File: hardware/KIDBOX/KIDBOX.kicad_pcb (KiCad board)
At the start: 2 copper layers, 150 x 65 mm, 0 parts

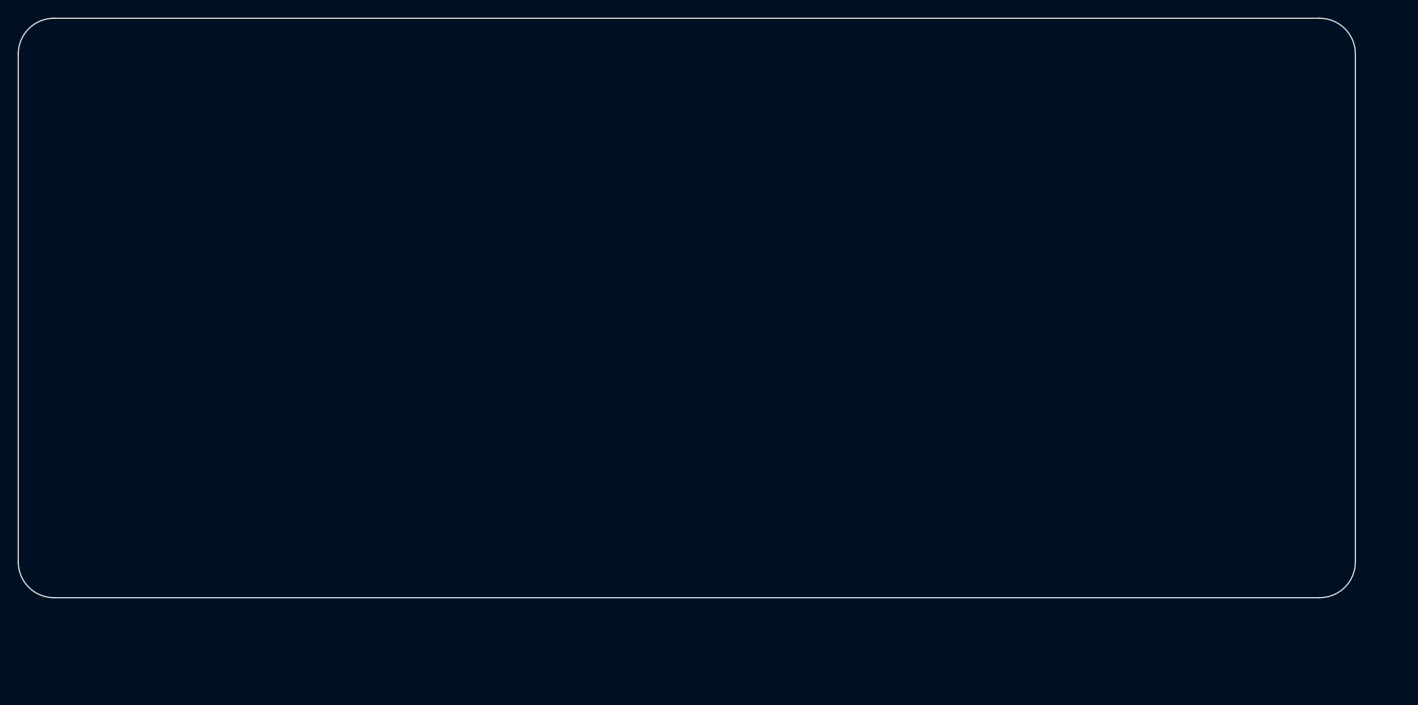
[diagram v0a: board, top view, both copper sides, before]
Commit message: Fase 2 PCB KIDBOX + correcciones de revision (sin H5/H6, SELECT/START a 66.5/83.5)
- scripts/gen_pcb.py: PCB completo generado con pcbnew (contorno 150x65 r4,
  H1-H4, huellas oficiales en las posiciones de la seccion 6, 0 vias, pistas
  en F.Cu, plano GND continuo en B.Cu con alivios termicos, serigrafia).
- J5 con VIN a la derecha visto de frente (I2S sin cruces ni vias); 3V3 a
  VIN por un puente pad a pad en B.Cu; PWR_EN por el borde superior.
- Revision del alumno: se eliminan H5/H6 y la regla de KIDBOX.kicad_dru;
  SW5/SW6 a x = 66.5 / 83.5 para sacar el cobre de START de la zona de bateria.
- verificar.py: ERC 0, DRC 0 errores / 0 avisos, 0 sin conectar, paridad 0.

Co-Authored-By: Claude Opus 5.5 <noreply@anthropic.com>
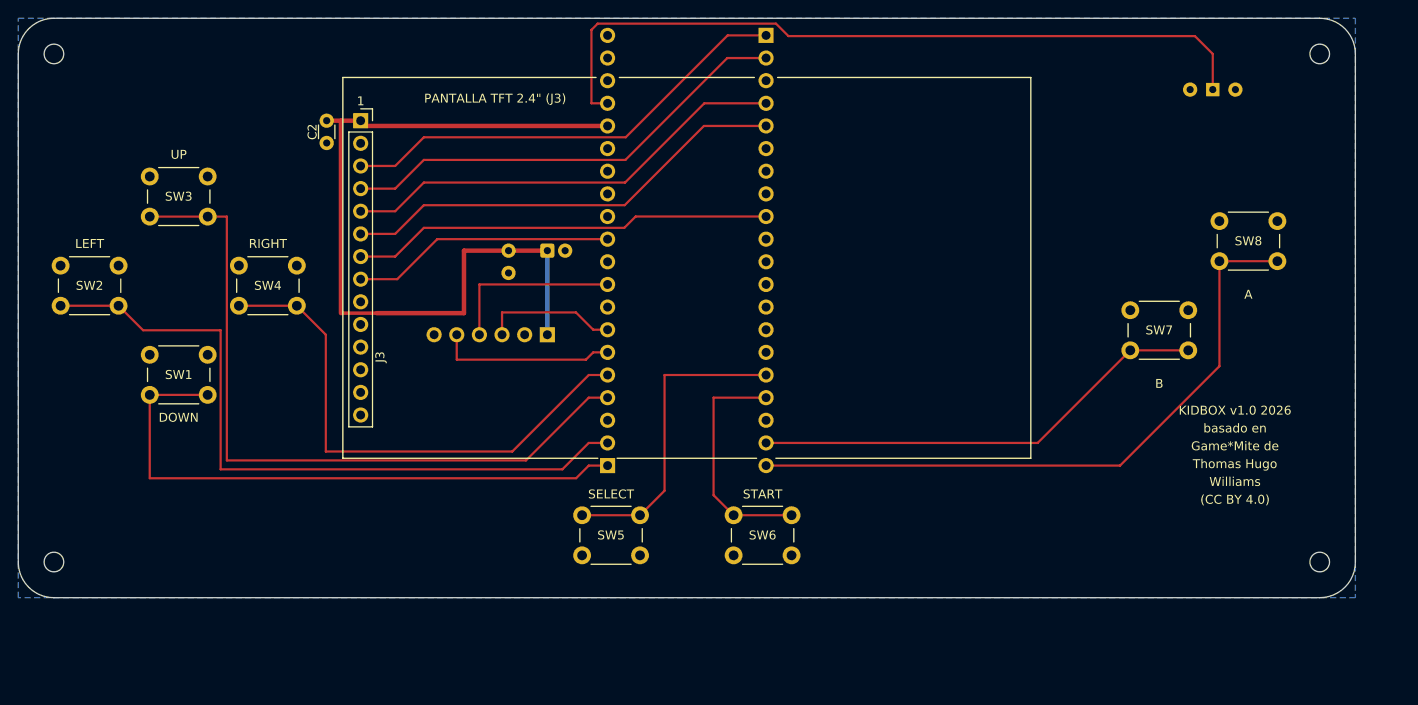
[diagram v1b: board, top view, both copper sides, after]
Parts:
- added C2: 100n, Capacitor_THT:C_Disc_D3.0mm_W1.6mm_P2.50mm, F.Cu at (34.6, 11.5)
- added C3: 100n, Capacitor_THT:C_Disc_D3.0mm_W1.6mm_P2.50mm, B.Cu at (55.0, 26.1)
- added C4: 10u 16V, Capacitor_THT:CP_Radial_D5.0mm_P2.00mm, B.Cu at (59.4, 26.1)
- added H1: M2, MountingHole:MountingHole_2.2mm_M2, F.Cu at (4.00, 4.00)
- added H2: M2, MountingHole:MountingHole_2.2mm_M2, F.Cu at (146.0, 4.00)
- added H3: M2, MountingHole:MountingHole_2.2mm_M2, F.Cu at (4.00, 61.0)
- added H4: M2, MountingHole:MountingHole_2.2mm_M2, F.Cu at (146.0, 61.0)
- added J1: RP2350-Plus 1-20, Connector_PinSocket_2.54mm:PinSocket_1x20_P2.54mm_Vertical, B.Cu at (83.9, 1.92)
- added J2: RP2350-Plus 21-40, Connector_PinSocket_2.54mm:PinSocket_1x20_P2.54mm_Vertical, B.Cu at (66.1, 50.2)
- added J3: TFT ILI9341 2.4in, Connector_PinSocket_2.54mm:PinSocket_1x14_P2.54mm_Vertical, F.Cu at (38.4, 11.5)
- added J5: DAC GY-PCM5102, Connector_PinSocket_2.54mm:PinSocket_1x06_P2.54mm_Vertical, B.Cu at (59.4, 35.5)
- added SW1: DOWN, Button_Switch_THT:SW_PUSH_6mm, F.Cu at (21.2, 42.2)
- added SW10: ON/OFF, Button_Switch_THT:SW_Slide-03_Wuerth-WS-SLTV_10x2.5x6.4_P2.54mm, B.Cu at (134.0, 8.00)
- added SW2: LEFT, Button_Switch_THT:SW_PUSH_6mm, F.Cu at (11.2, 32.2)
- added SW3: UP, Button_Switch_THT:SW_PUSH_6mm, F.Cu at (21.2, 22.2)
- added SW4: RIGHT, Button_Switch_THT:SW_PUSH_6mm, F.Cu at (31.2, 32.2)
- added SW5: SELECT, Button_Switch_THT:SW_PUSH_6mm, F.Cu at (63.2, 55.8)
- added SW6: START, Button_Switch_THT:SW_PUSH_6mm, F.Cu at (80.2, 55.8)
- added SW7: B, Button_Switch_THT:SW_PUSH_6mm, F.Cu at (131.2, 37.2)
- added SW8: A, Button_Switch_THT:SW_PUSH_6mm, F.Cu at (141.2, 27.2)
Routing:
- net +3V3: track 0.00 -> 92.9 mm
- net /PWR_EN: track 0.00 -> 85.4 mm
- net /BTN_UP: track 0.00 -> 81.6 mm
- net /BTN_LEFT: track 0.00 -> 79.3 mm
- net /BTN_A: track 0.00 -> 73.8 mm
- net /BTN_DOWN: track 0.00 -> 67.8 mm
- net /BTN_RIGHT: track 0.00 -> 59.4 mm
- net /BTN_B: track 0.00 -> 51.7 mm
- net /LCD_RST: track 0.00 -> 51.5 mm
- net /LCD_CS: track 0.00 -> 51.5 mm
- net /LCD_MOSI: track 0.00 -> 50.5 mm
- net /LCD_DC: track 0.00 -> 50.5 mm
- net /LCD_SCK: track 0.00 -> 47.3 mm
- net /BTN_SELECT: track 0.00 -> 34.8 mm
- net /LCD_LED: track 0.00 -> 29.6 mm
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- added copper zone on B.Cu, net GND
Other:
- board text added: "(CC BY 4.0)"
- board text added: "1"
- board text added: "A"
- board text added: "B"
- board text added: "BATERÍA 103450"
- board text added: "BOOT/RST"
- board text added: "DAC PCM5102"
- board text added: "DOWN"
- board text added: "FILAS ESPEJADAS"
- board text added: "GND"
- board text added: "Game*Mite de"
- board text added: "JACK"
- board text added: "KIDBOX v1.0 2026"
- board text added: "LEFT"
- board text added: "ON/OFF"
- board text added: "PANTALLA TFT 2.4" (J3)"
- board text added: "RIGHT"
- board text added: "RP2350-Plus"
- board text added: "SELECT"
- board text added: "START"
- board text added: "Thomas Hugo"
- board text added: "UP"
- board text added: "USB-C"
- board text added: "VIN"
- board text added: "VISTA POSTERIOR"
- board text added: "Williams"
- board text added: "basado en"
- board text added: "sin patas THT"

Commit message: Fase 4: fabricacion PRELIMINAR
Paquete para JLCPCB (2 capas) en fabricacion/: Gerbers, taladros Excellon
(PTH/NPTH separados, origen absoluto, mapas PDF), KIDBOX_gerbers_PRELIMINAR.zip
y PDF 1:1 de frente y reverso; README.md con el aviso PRELIMINAR - NO FABRICAR,
orden de soldadura, parametros de pedido y revision en el visor.

Incluye las correcciones de la Fase 3 (rondas 2 y 3): DAC horizontal (J5 en
x = 59, C3/C4, I2S y 3V3 re-ruteados, sin pistas en B.Cu), min_connection 0.2,
C4 10u 25V, huellas con hoja/filtros/unidades (F8 sin cambios), OFF/ON en SW10,
KIDBOX/.history/ en .gitignore, verificar_extra.py y la especificacion
actualizada por el alumno. El .kicad_pcb no cambio en la Fase 4.

Co-Authored-By: Claude Opus 5.5 <noreply@anthropic.com>
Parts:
- C4: value 10u 16V -> 10u 25V
- moved C3 37.6 mm to (60.6, 63.3), turned to 180 degrees
- moved C4 36.0 mm to (74.0, 59.0)
- moved J5 24.3 mm to (59.0, 59.8), turned to 0 degrees
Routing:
- net +3V3: track 92.9 -> 150.9 mm
- net /I2S_LRCK: track 15.1 -> 35.5 mm
- net /I2S_DIN: track 20.0 -> 35.2 mm
- net /I2S_BCK: track 20.1 -> 25.6 mm
- net /BTN_DOWN: track 67.8 -> 71.6 mm
- net /BTN_LEFT: track 79.3 -> 81.4 mm
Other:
- board text added: "OFF"
- board text added: "ON"
- board text removed: "ON/OFF"

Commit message: Fase 4: BOM al dia y ubicacion del numero de pedido
- BOM: nota de SW10 "paso 2.54 mm confirmado en protoboard (14-oct)";
  DECISIONES.md marca como resueltos el paso de SW10 y el orden de J5.
- B.SilkS: "JLCJLCJLCJLC" (1.0 mm) dentro de la zona de bateria, en (102.5, 33)
  vertical, sin tocar "BATERIA 103450"; README: Order number: Specify a location.
- Gerbers y zip regenerados. verificar.py y verificar_extra.py sin errores.

Co-Authored-By: Claude Opus 5.5 <noreply@anthropic.com>
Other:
- board text added: "JLCJLCJLCJLC"

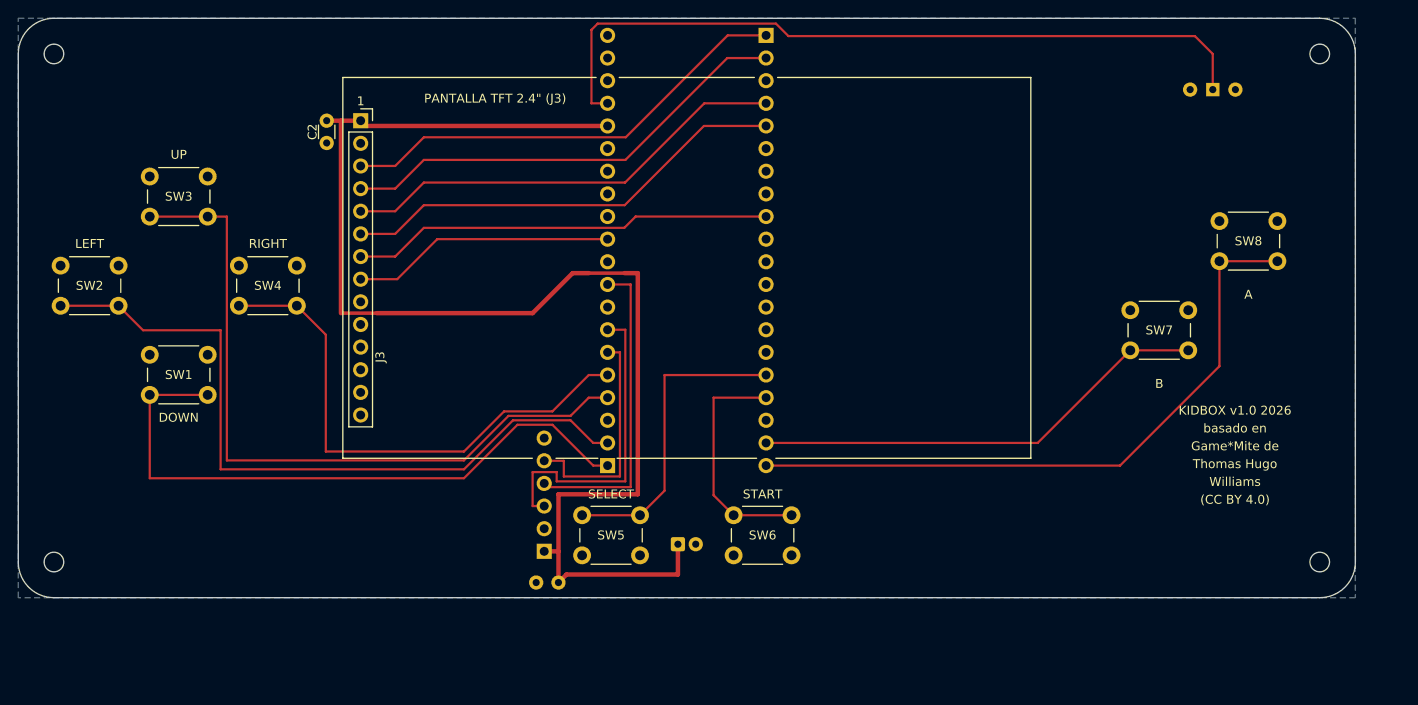
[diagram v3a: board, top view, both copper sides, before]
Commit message: v0.8: pantalla +3 mm, DAC hacia la cruceta, C3 al costado de J5
Co-Authored-By: Claude Opus 5.5 <noreply@anthropic.com>
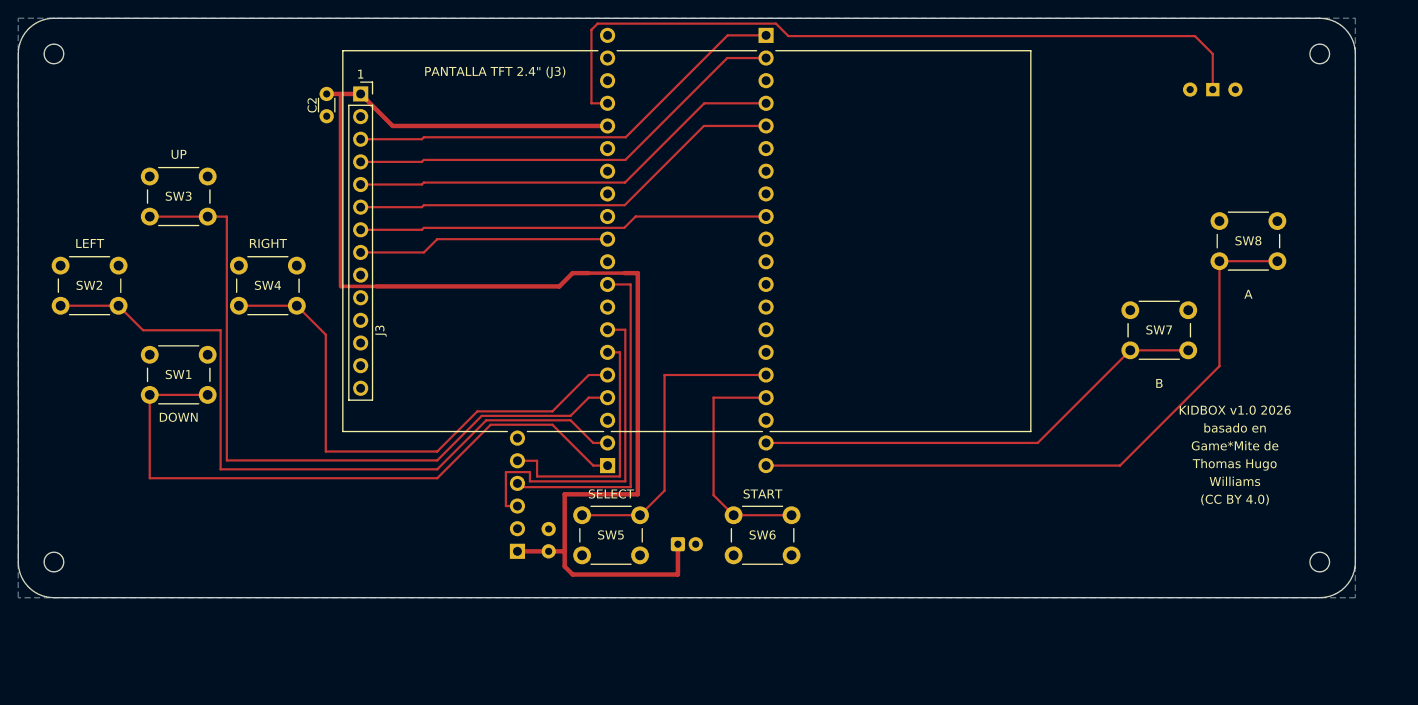
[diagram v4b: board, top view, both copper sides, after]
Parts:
- moved C3 3.67 mm to (59.5, 59.8), turned to 90 degrees
- moved C2 3.00 mm to (34.6, 8.49)
- moved J3 3.00 mm to (38.4, 8.49)
- moved J5 3.00 mm to (56.0, 59.8)
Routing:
- net /I2S_LRCK: track 35.5 -> 38.5 mm
- net /I2S_DIN: track 35.2 -> 38.2 mm
- net /I2S_BCK: track 25.6 -> 28.6 mm
- net /LCD_SCK: track 47.3 -> 46.1 mm
- net /LCD_RST: track 51.5 -> 50.3 mm
- net /LCD_MOSI: track 50.5 -> 49.3 mm
- net /LCD_LED: track 29.6 -> 28.3 mm
- net /LCD_DC: track 50.5 -> 49.3 mm
- net /LCD_CS: track 51.5 -> 50.3 mm

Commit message: v0.8: C2 y C3 con huella de paso 5 mm
Co-Authored-By: Claude Opus 5.5 <noreply@anthropic.com>
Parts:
- C2, C3: footprint Capacitor_THT:C_Disc_D3.0mm_W1.6mm_P2.50mm -> Capacitor_THT:C_Disc_D5.0mm_W2.5mm_P5.00mm

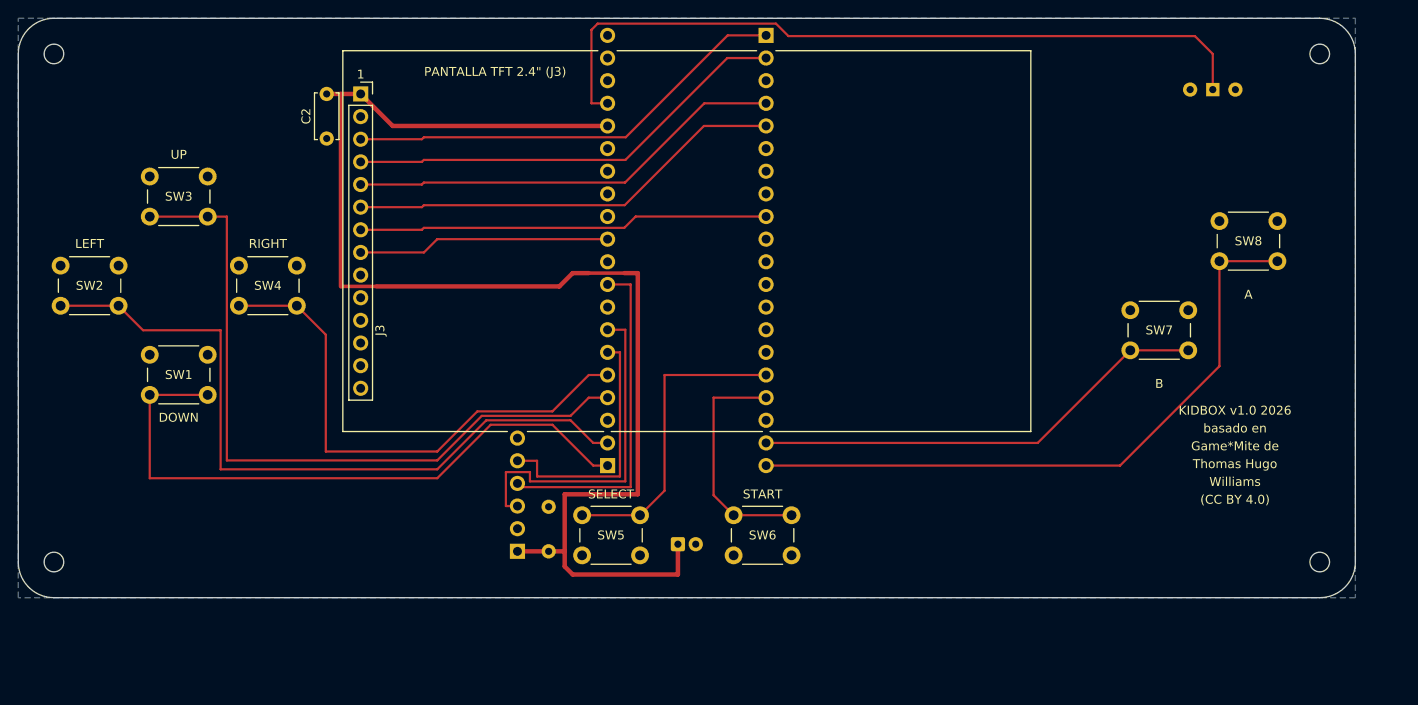
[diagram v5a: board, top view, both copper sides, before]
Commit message: v0.9: 155x75, simetría, imagen centrada, DAC adelante, correcciones del profesor
- Placa 155 x 75 (r = 4), agujeros M2 en (4,4), (151,4), (4,71), (151,71); eje de simetría x = 77.5.
- Imagen de la pantalla centrada (módulo en x = 73.5, J3 en x = 36.91); RP2350-Plus centrado (68.61 / 86.39);
  zona de batería x 90.5-126.0.
- DAC adelante con huella propia Connector_KIDBOX:GY-PCM5102_1x06_P2.54mm (KIDBOX/KIDBOX.pretty, gen_huella_dac.py):
  jack centrado en x = 77.5 con la boca en y = 75; C3 y C4 junto a VIN, fuera del DAC.
- Controles simétricos: cruceta (18, 44), A/B (142, 39)/(132, 49), SELECT/START (41, 67)/(114, 67); SW10 atrás en (50, 8).
- Correcciones del profesor: 3V3 sin pasar entre pines de J3 (0.25 mm en J2), LRCK fuera de J5 (cruza J2.30/J2.29),
  BCK a 0.85 mm de J2.21, reglas .kicad_dru de 0.29 mm, C4 en CP_Radial_D4.0mm_P1.50mm, TP1/TP2, BT1 excluida de la
  placa, PWR_EN lejos del borde, rótulos 1.2/0.18, v0.9 en serigrafía, cajetín, README y zip.
- BOM de compra completa (BOM_compra.csv), PDF 1:1 en A4 y Carta, carpeta de entrega (gen_entrega.py).
- ESPECIFICACION.md v0.9, DECISIONES.md sección 16, README reescrito.

verificar.py: SIN ERRORES (ERC 0/0, DRC 0/0, sin conectar 0, paridad 0).
verificar_extra.py: 0 con los tests ignorados activados; F8 en seco 0 cambios.

Co-Authored-By: Claude Opus 5.5 <noreply@anthropic.com>
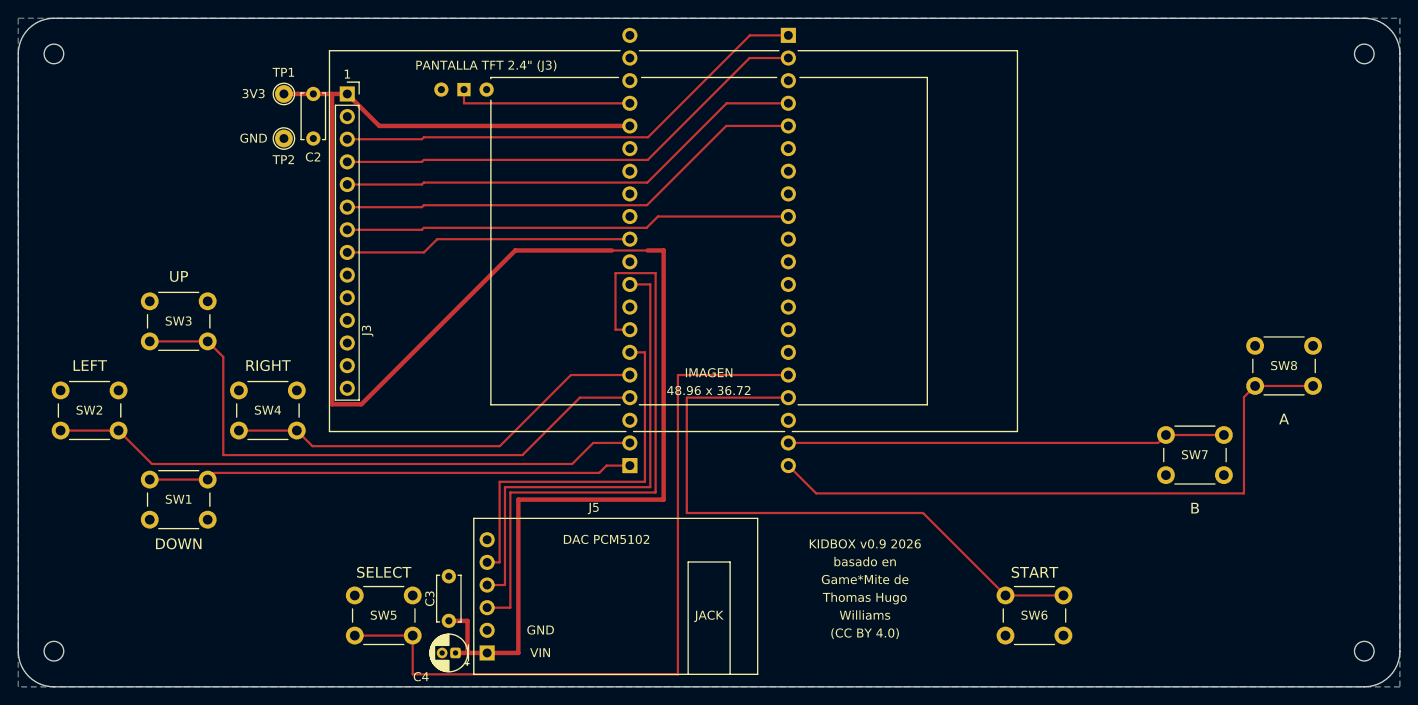
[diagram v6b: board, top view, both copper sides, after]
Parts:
- added SW7: B, Button_Switch_THT:SW_PUSH_6mm, F.Cu at (128.8, 46.8)
- added TP2: GND, TestPoint:TestPoint_THTPad_D2.0mm_Drill1.0mm, F.Cu at (29.8, 13.5)
- C3: moved to F.Cu
- C4: footprint Capacitor_THT:CP_Radial_D5.0mm_P2.00mm -> Capacitor_THT:CP_Radial_D4.0mm_P1.50mm; moved to F.Cu
- J5: footprint Connector_PinSocket_2.54mm:PinSocket_1x06_P2.54mm_Vertical -> Connector_KIDBOX:GY-PCM5102_1x06_P2.54mm; moved to F.Cu
- TP1: renamed from SW7; value B -> 3V3; footprint Button_Switch_THT:SW_PUSH_6mm -> TestPoint:TestPoint_THTPad_D2.0mm_Drill1.0mm
- moved TP1 105.4 mm to (29.8, 8.49), turned to 0 degrees
- moved SW10 84.0 mm to (50.0, 8.00)
- moved SW6 31.8 mm to (110.8, 64.8)
- moved C4 27.8 mm to (49.0, 71.2), turned to 180 degrees
- moved SW5 23.3 mm to (44.2, 69.2), turned to 180 degrees
- moved SW8 14.6 mm to (145.2, 41.2)
- moved SW2 14.0 mm to (11.2, 46.2)
- moved SW3 14.0 mm to (21.2, 36.2)
- moved SW4 14.0 mm to (31.2, 46.2)
- moved C3 13.6 mm to (48.3, 67.6)
- moved J5 11.9 mm to (52.6, 71.2)
- moved SW1 11.5 mm to (14.8, 51.8), turned to 0 degrees
- moved H4 11.2 mm to (151.0, 71.0)
- moved H3 10.0 mm to (4.00, 71.0)
- moved H2 5.00 mm to (151.0, 4.00)
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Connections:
- TP1 pad 1: /BTN_B -> +3V3
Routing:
- net /PWR_EN: track 85.4 -> 20.1 mm
- net /BTN_SELECT: track 34.8 -> 86.6 mm
- net /BTN_START: track 26.5 -> 70.4 mm
- net +3V3: track 151.4 -> 193.7 mm
- net /I2S_LRCK: track 38.5 -> 68.9 mm
- net /BTN_DOWN: track 71.6 -> 54.5 mm
- net /I2S_DIN: track 38.2 -> 54.3 mm
- net /BTN_LEFT: track 81.4 -> 66.4 mm
- net /I2S_BCK: track 28.6 -> 42.9 mm
- net /BTN_UP: track 81.6 -> 68.3 mm
- net /BTN_RIGHT: track 59.4 -> 47.9 mm
- net /LCD_SCK: track 46.1 -> 50.1 mm
- net /LCD_RST: track 50.3 -> 54.3 mm
- net /LCD_MOSI: track 49.3 -> 53.3 mm
- net /LCD_DC: track 49.3 -> 53.3 mm
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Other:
- board size 150 x 65 mm -> 155 x 75 mm
- board text added: "155 x 75 mm - 1.6 mm - 2 capas"
- board text added: "3V3"
- board text added: "48.96 x 36.72"
- board text added: "IMAGEN"
- board text added: "KIDBOX v0.9 - 26-oct-2026"
- board text added: "KIDBOX v0.9 2026"
- board text removed: "KIDBOX v1.0 2026"
